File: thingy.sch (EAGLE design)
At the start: 24 parts, among them IC1 MCP6001T-I/OT, IC2 MAX9812LEXT+T, IC3 ESP-12, IC4 ADXL345BCCZ, J1 Interface, J2 GPIO, J3 Interrupts, Q1 Electret Mic

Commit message: Add files via upload
wat is dis how 2 pley guise?
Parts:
- added CX1, CX2: 1UF/X7R, rcl:CXXC10B5
- added R13: 100k, resistor:R-EU_R0603
- added U1: RT9013-XXXB, v-reg-new:RT9013-XXXB
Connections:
- new net 1UF/X7R: CX1.2
- new net N$3: CX2.1, CX2.2
- new net N$5: R13.2
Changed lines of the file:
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@@
 <?xml version="1.0" encoding="utf-8"?>
 <!DOCTYPE eagle SYSTEM "eagle.dtd">
-<eagle version="6.5.0">
+<eagle version="7.7.0">
 <drawing>
 <settings>
@@
 <setting verticaltext="up"/>
 </settings>
-<grid distance="0.1" unitdist="inch" unit="inch" style="lines" multiple="1" display="yes" altdistance="0.01" altunitdist="inch" altunit="inch"/>
+<grid distance="0.1" unitdist="inch" unit="inch" style="lines" multiple="1" display="no" altdistance="0.01" altunitdist="inch" altunit="inch"/>
 <layers>
 <layer number="1" name="Top" color="4" fill="1" visible="no" active="no"/>
@@
 </part>
 <part name="U$1" library="freetronics-luke" deviceset="GND" device=""/>
+<part name="U1" library="v-reg-new" deviceset="RT9013-XXX" device="B"/>
+<part name="CX1" library="rcl" deviceset="CX" device="XC10B5" value="1UF/X7R"/>
+<part name="CX2" library="rcl" deviceset="CX" device="XC10B5" value="1UF/X7R"/>
+<part name="R13" library="resistor" deviceset="R-EU_" device="R0603" value="100k"/>
 </parts>
 <sheets>
@@
 </instance>
 <instance part="U$1" gate="G$1" x="91.44" y="22.86" rot="MR0"/>
+<instance part="U1" gate="G$1" x="53.34" y="124.46"/>
+<instance part="CX1" gate="G$1" x="38.1" y="134.62"/>
+<instance part="CX2" gate="G$1" x="71.12" y="127"/>
+<instance part="R13" gate="G$1" x="38.1" y="119.38" rot="R90"/>
 </instances>
 <busses>
@@
 </segment>
 </net>
+<net name="1UF/X7R" class="0">
+<segment>
+<wire x1="45.72" y1="129.54" x2="38.1" y2="129.54" width="0.1524" layer="91"/>
+<wire x1="38.1" y1="129.54" x2="30.48" y2="129.54" width="0.1524" layer="91"/>
+<wire x1="38.1" y1="129.54" x2="38.1" y2="134.62" width="0.1524" layer="91"/>
+<pinref part="CX1" gate="G$1" pin="2"/>
+<junction x="38.1" y="129.54"/>
+</segment>
+</net>
+<net name="N$3" class="0">
+<segment>
+<wire x1="60.96" y1="129.54" x2="71.12" y2="129.54" width="0.1524" layer="91"/>
+<wire x1="78.74" y1="129.54" x2="71.12" y2="129.54" width="0.1524" layer="91"/>
+<wire x1="71.12" y1="129.54" x2="71.12" y2="121.92" width="0.1524" layer="91"/>
+<pinref part="CX2" gate="G$1" pin="1"/>
+<junction x="71.12" y="129.54"/>
+<pinref part="CX2" gate="G$1" pin="2"/>
+</segment>
+</net>
+<net name="N$4" class="0">
+<segment>
+<wire x1="60.96" y1="124.46" x2="66.04" y2="124.46" width="0.1524" layer="91"/>
+</segment>
+</net>
+<net name="N$5" class="0">
+<segment>
+<wire x1="45.72" y1="124.46" x2="38.1" y2="124.46" width="0.1524" layer="91"/>
+<wire x1="38.1" y1="124.46" x2="30.48" y2="124.46" width="0.1524" layer="91"/>
+<wire x1="38.1" y1="124.46" x2="38.1" y2="119.38" width="0.1524" layer="91"/>
+<pinref part="R13" gate="G$1" pin="2"/>
+<junction x="38.1" y="124.46"/>
+</segment>
+</net>
+<net name="N$6" class="0">
+<segment>
+<wire x1="53.34" y1="116.84" x2="53.34" y2="111.76" width="0.1524" layer="91"/>
+</segment>
+</net>

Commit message: Add files via upload
This can't be right..
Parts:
- removed C5: 100nF, freetronics-luke:C0603
- removed IC1: MCP6001T-I/OT, burr-brown:OPA340N
- removed IC4: ADXL345BCCZ, SparkFun:ADXL345
- removed J3: Interrupts, pinhead:PINHD-1X2
- removed R10, R11: 4.7kΩ, freetronics-luke:R0603
- removed R2: 62kΩ, freetronics-luke:R0603
- removed R3: 27kΩ, freetronics-luke:R0603
- added C6, C8: 100nF, SparkFun:CAP0402-CAP
- added C7: 10nF, SparkFun:CAP0402-CAP
- added C9: 2,2nF, SparkFun:CAP0402-CAP
- added IC5: MPU-6050, seb:MPU-6050
- added JP1: (no value), pinhead-2:PINHD-1X05_2.54
- added R14, R5: (no value), SparkFun:RESISTOR0402-RES
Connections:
- removed net ACC_INT1: IC4.INT1, J3.1
- removed net ACC_INT2: IC4.INT2, J3.2
- removed net N$11: IC1.+IN, R2.1, R3.2
- removed net N$3: CX2.1, CX2.2
- new net +3V3: C7.2, C8.1, IC5.13, IC5.8, JP1.2, R14.2, R5.2
- new net INT: IC5.12, JP1.3
- new net N$2: C6.2, IC5.10
- new net N$8: C9.1, IC5.20
- new net SCL1: IC5.23, JP1.4, R5.1
- new net SDA1: IC5.24, JP1.5, R14.1
- net +3.3V: no longer C5.1, IC1.V+, IC4.CS, IC4.SDO, IC4.VDD, IC4.VSS, R10.2, R11.2, R2.2
- net GND: now also C6.1, C7.1, C8.2, C9.2, IC5.1, IC5.11, IC5.18, IC5.9, IC5.P, JP1.1; no longer C5.2, IC1.V-, IC4.GND, IC4.GND1, IC4.GND2, R3.1
- net N$1: now also CX2.1, CX2.2; no longer IC1.-IN, IC1.OUT
- net SCL: no longer IC4.SCL, R11.1
- net SDA: no longer IC4.SDA, R10.1
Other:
- note removed: "NC"
- note removed: "Vs not VSS"

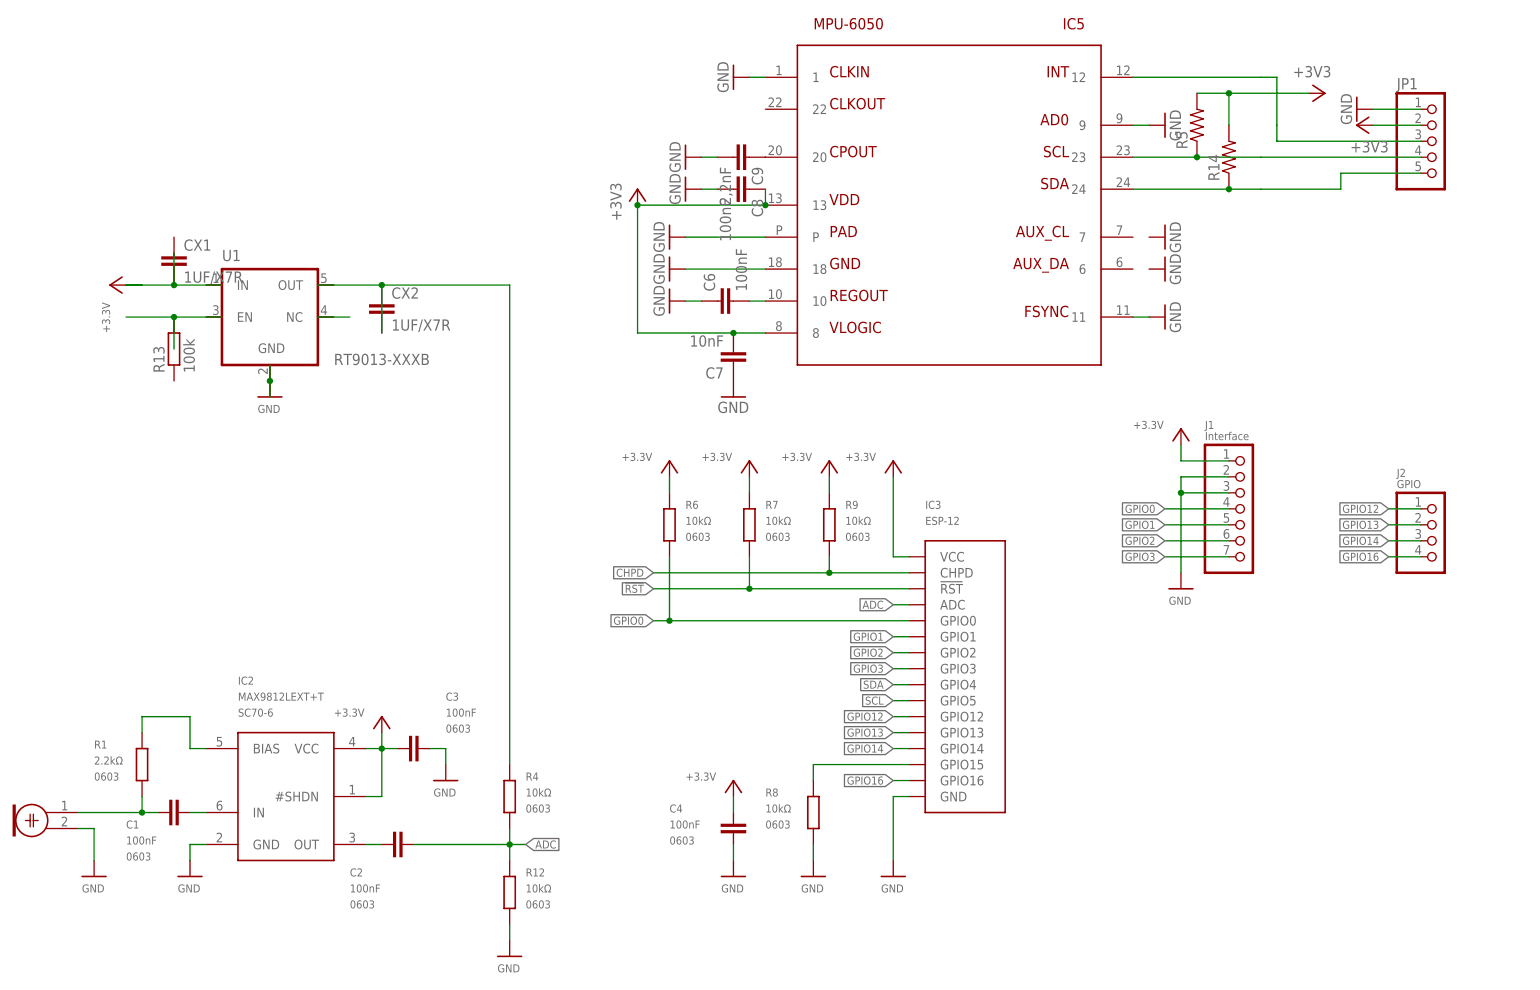
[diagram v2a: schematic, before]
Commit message: Add files via upload
Added the MCP6001 back in woopsie
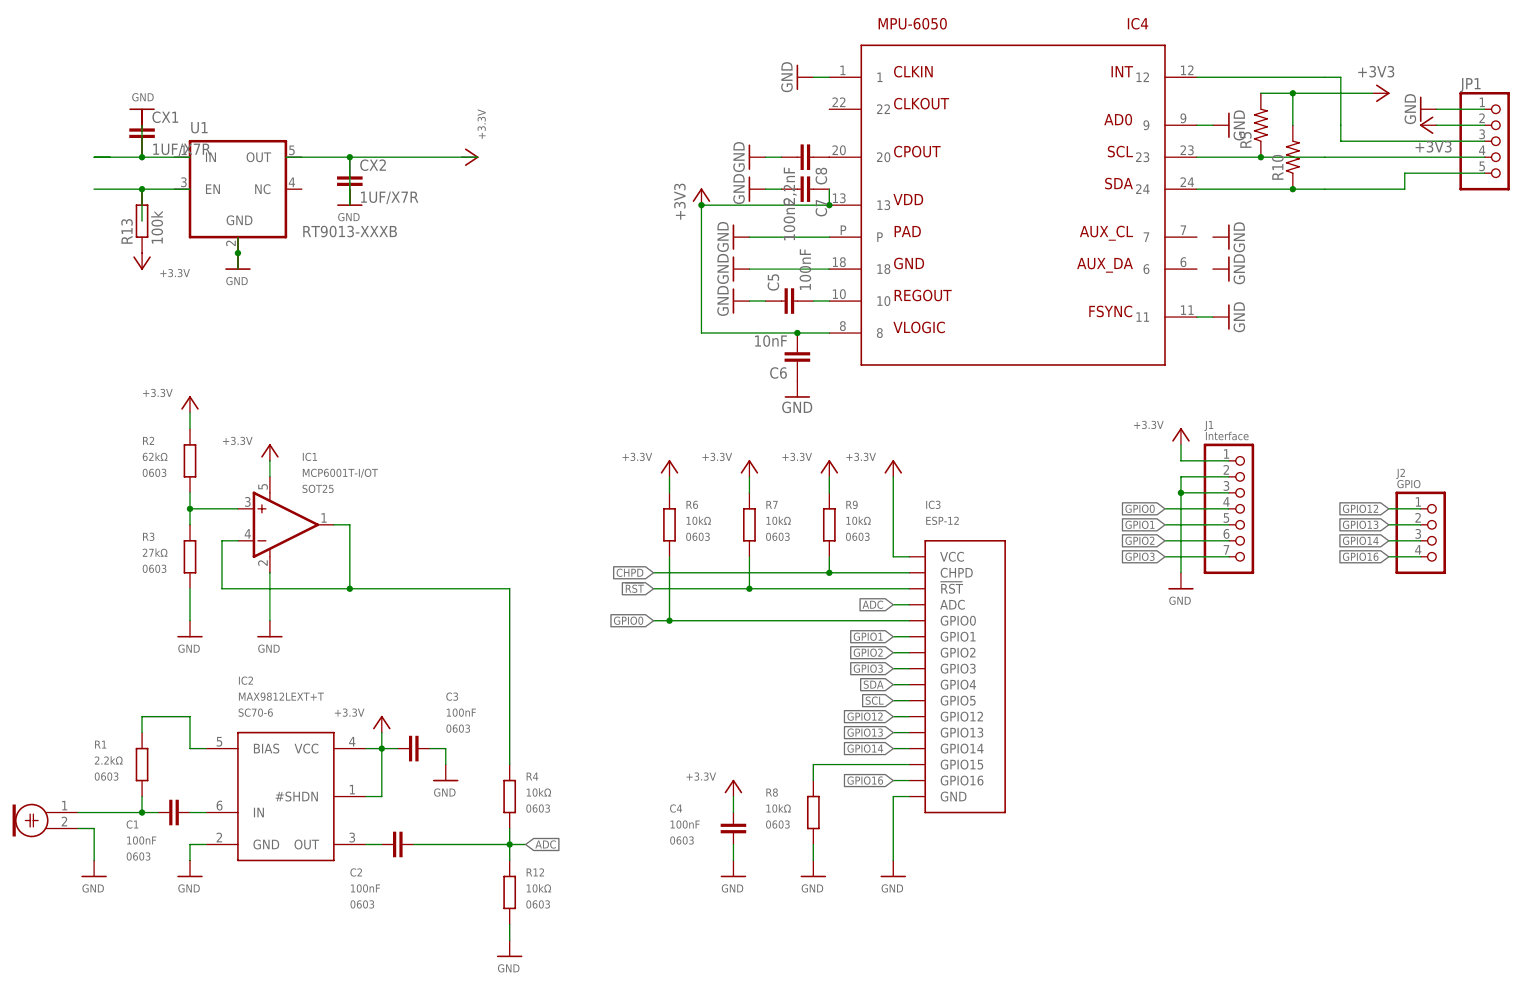
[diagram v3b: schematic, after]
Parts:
- removed C9: 2,2nF, SparkFun:CAP0402-CAP
- removed IC5: MPU-6050, seb:MPU-6050
- removed R14: (no value), SparkFun:RESISTOR0402-RES
- added C5: 100nF, SparkFun:CAP0402-CAP
- added IC1: MCP6001T-I/OT, burr-brown:OPA340N
- added IC4: MPU-6050, seb:MPU-6050
- added R10: (no value), SparkFun:RESISTOR0402-RES
- added R2: 62kΩ, freetronics-luke:R0603
- added R3: 27kΩ, freetronics-luke:R0603
- C6: value 100nF -> 10nF
- C7: value 10nF -> 100nF
- C8: value 100nF -> 2,2nF
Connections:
- removed net N$8: C9.1, IC5.20
- new net N$11: IC1.+IN, R2.1, R3.2
- new net N$3: C8.1, IC4.20
- new net N$4: CX2.1, CX2.2
- net +3.3V: now also IC1.V+, R2.2
- net +3V3: now also C6.2, C7.1, IC4.13, IC4.8, R10.2; no longer C7.2, C8.1, IC5.13, IC5.8, R14.2
- net GND: now also C5.1, C7.2, IC1.V-, IC4.1, IC4.11, IC4.18, IC4.9, IC4.P, R3.1; no longer C7.1, C9.2, IC5.1, IC5.11, IC5.18, IC5.9, IC5.P
- net INT: now also IC4.12; no longer IC5.12
- net N$1: now also IC1.-IN, IC1.OUT; no longer CX2.1, CX2.2
- net N$2: now also C5.2, IC4.10; no longer C6.2, IC5.10
- net SCL1: now also IC4.23; no longer IC5.23
- net SDA1: now also IC4.24, R10.1; no longer IC5.24, R14.1
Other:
- moved on the sheet: C6, C7, C8, CX1, CX2, JP1, R13, R5, U1
